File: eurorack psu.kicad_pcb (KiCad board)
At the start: 2 copper layers, 100 x 59.5 mm, 30 parts, among them J1 Screw Terminal 1x3, J2 Screw_Terminal_01x03, M3 MountingHole_3.2mm_M3_DIN965_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, U1 LM7812, U2 LM7912

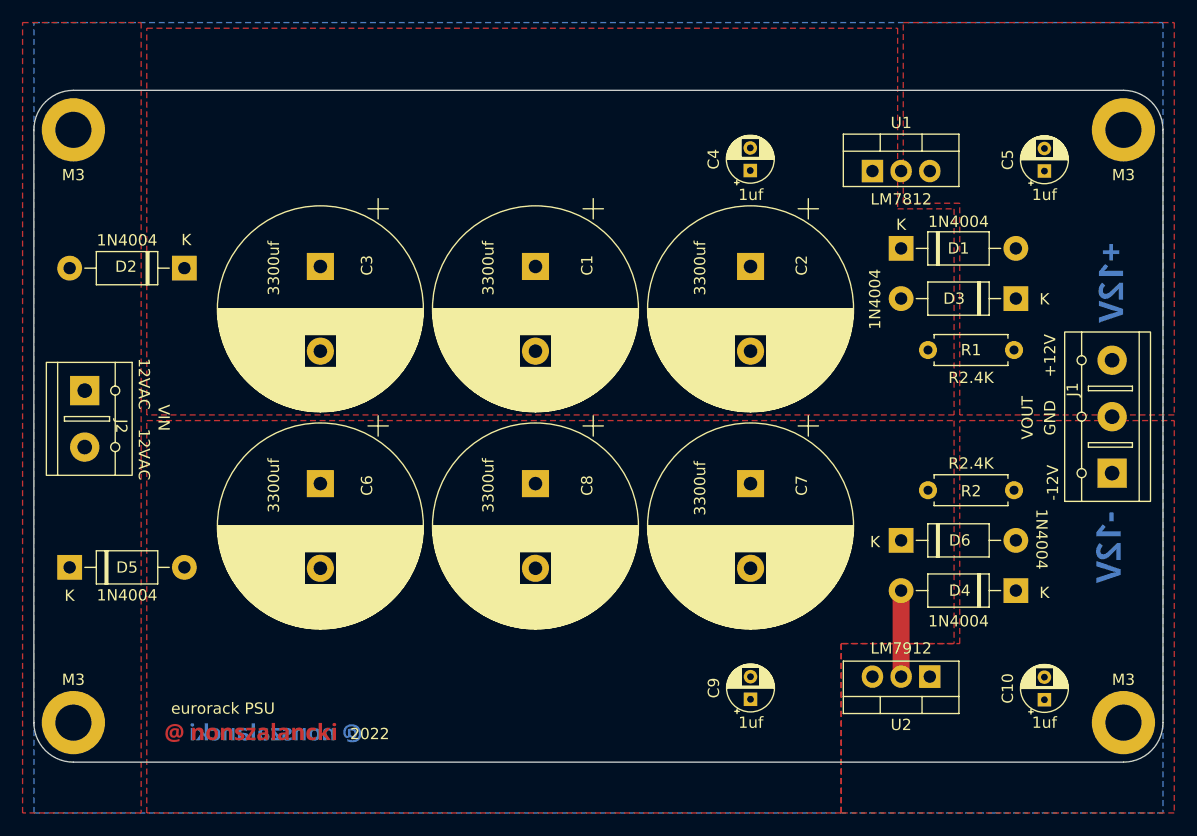
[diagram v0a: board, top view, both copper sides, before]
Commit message: silkscreen changes
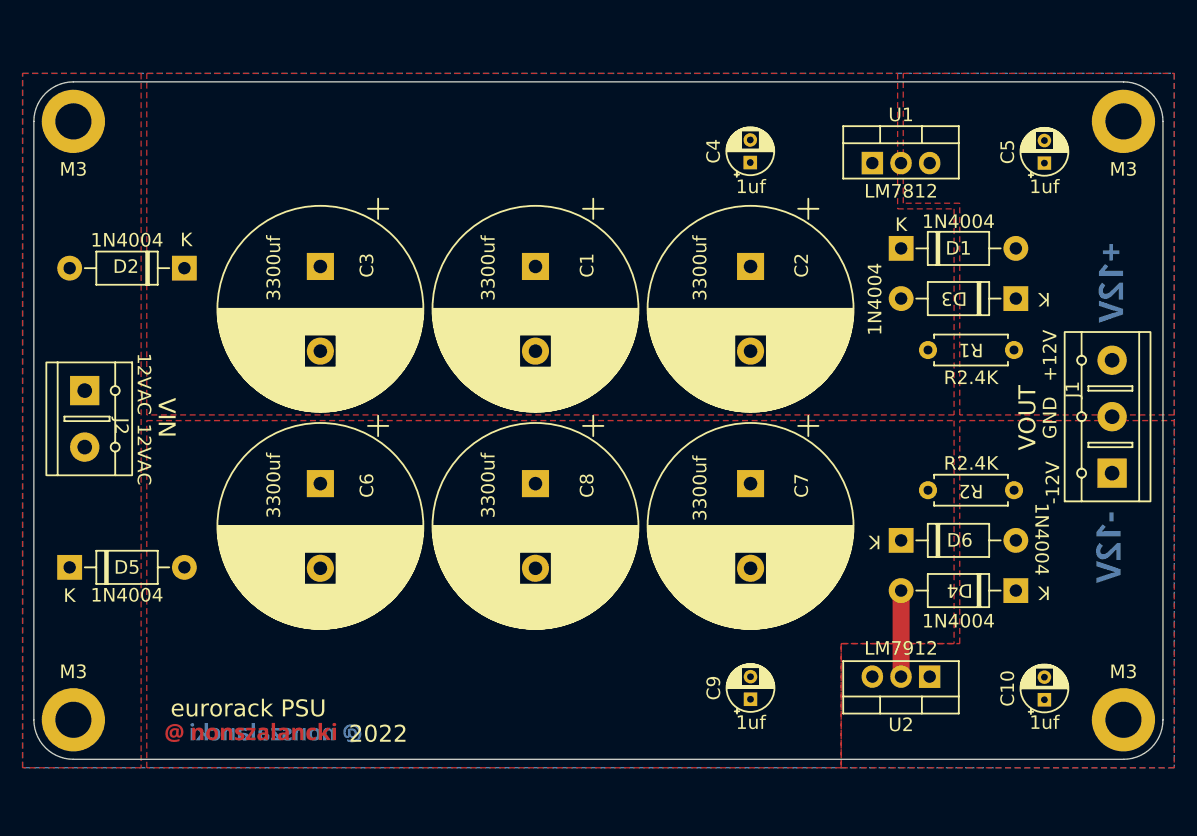
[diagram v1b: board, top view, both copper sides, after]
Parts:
- moved M3 0.75 mm to (151.5, 49.8)
- moved M3 0.75 mm to (58.5, 49.8)
- moved U1 0.71 mm to (129.3, 53.4)
- moved C4 0.71 mm to (118.5, 53.4)
- moved C5 0.70 mm to (144.5, 53.4)
- moved M3 0.25 mm to (58.5, 102.8)
- moved M3 0.25 mm to (151.5, 102.8)
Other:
- board size 100 x 59.5 mm -> 100 x 60 mm

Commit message: silkscreen changes
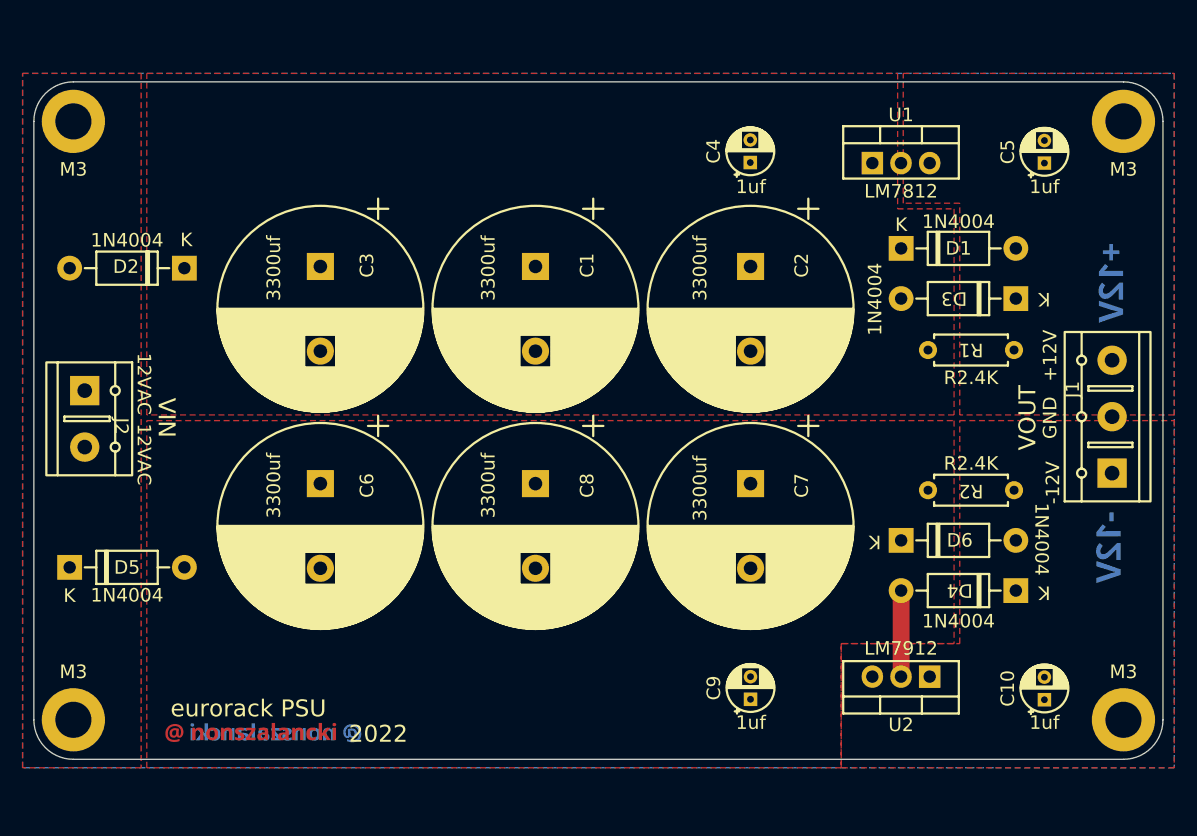
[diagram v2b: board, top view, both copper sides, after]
